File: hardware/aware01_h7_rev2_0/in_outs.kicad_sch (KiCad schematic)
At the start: 30 parts, among them J3 InL, J4 InR, J5 OutL, J6 OutR, U10 NE5532DRG4, U11 NE5532DRG4

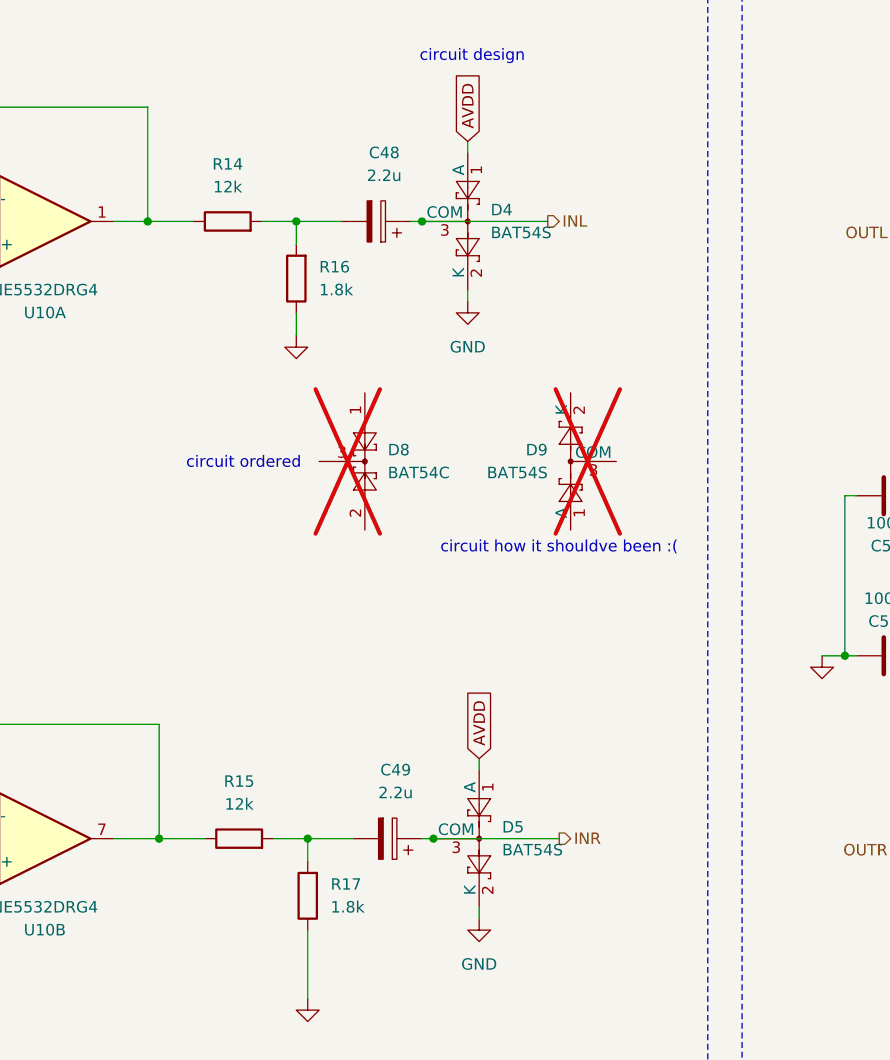
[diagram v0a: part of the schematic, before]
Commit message: feat: fixes in pcb design
- use correct BAT54S placement/layout
- fix pin mapping of fade potentiometers, also adjust routing
- switch pins that did not support PWM out (for fader led)
- switch pins that did not support EXTI
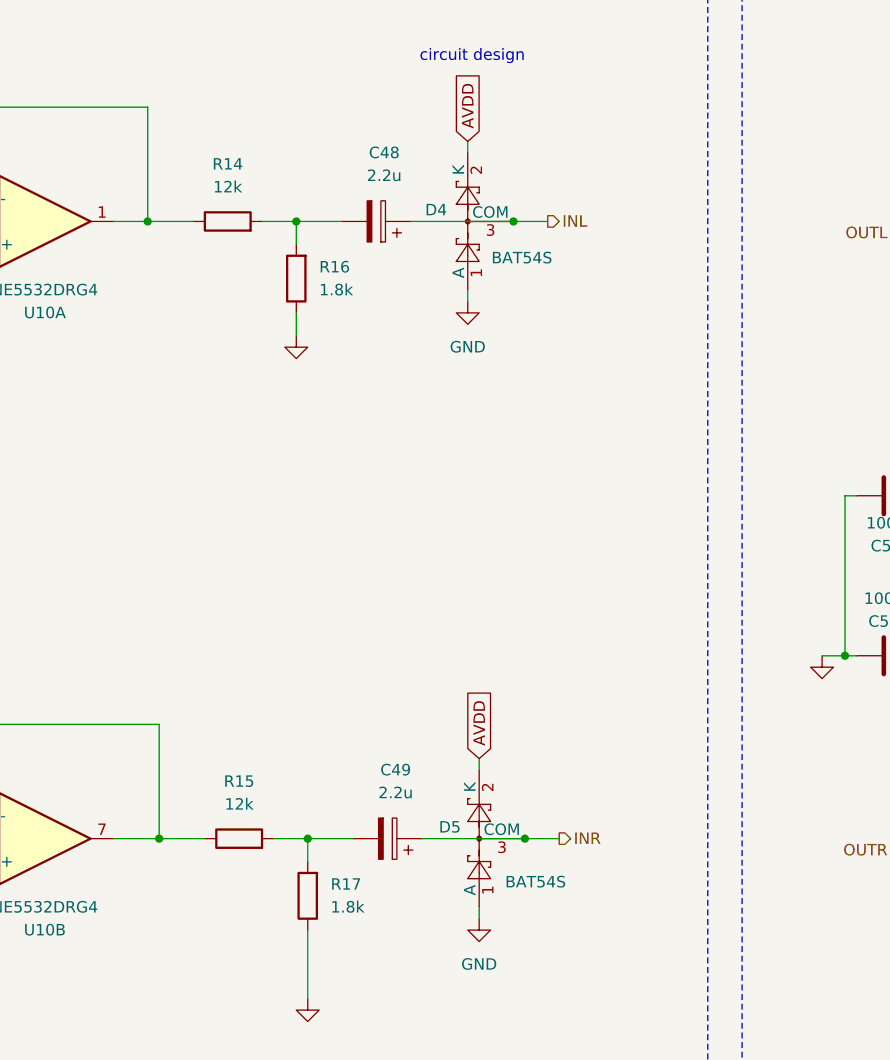
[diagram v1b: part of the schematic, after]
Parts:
- removed D4: BAT54S, Package_TO_SOT_SMD:SOT-23, symbol Diode:BAT54S
- removed D8: BAT54C, Package_TO_SOT_SMD:SOT-23, symbol Diode:BAT54C
- D4: renamed from D9; now fitted; now in the parts list
- D5: Manufacturer_Name Vishay Semiconductors -> (none); Manufacturer_Part_Number BAT54C-E3-08 -> (none); Mouser Part Number 78-BAT54C-E3-08 -> (none)
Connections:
- net AVDD: now also D4.2 (K), D5.2 (K); no longer D5.1 (A)
- net GND: now also D4.1 (A), D5.1 (A); no longer D5.2 (K)
- net INL: now also D4.3 (COM)
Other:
- note removed: "circuit how it shouldve been :("
- note removed: "circuit ordered"
